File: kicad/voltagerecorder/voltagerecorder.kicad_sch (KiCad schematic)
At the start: 87 parts, among them J1 Conn_02x10_Odd_Even, J10 Conn_01x02, J11 USB_C_Receptacle_USB2.0, J12 USB_C_Receptacle_USB2.0, J14 Conn_01x08, J15 Conn_01x02, J2 Conn_01x05, J3 Conn_01x08, J8 Conn_01x05, P1 DM3CS-SF, SW1 SW_Push, U1 Opamp_Quad, U5 ADS8638, U6 STM32G473CBT6, U8 ESP32-C3-WROOM-02, U9 ESP-PSRAM32, Y1 32.768kHz, Y2 24MHz

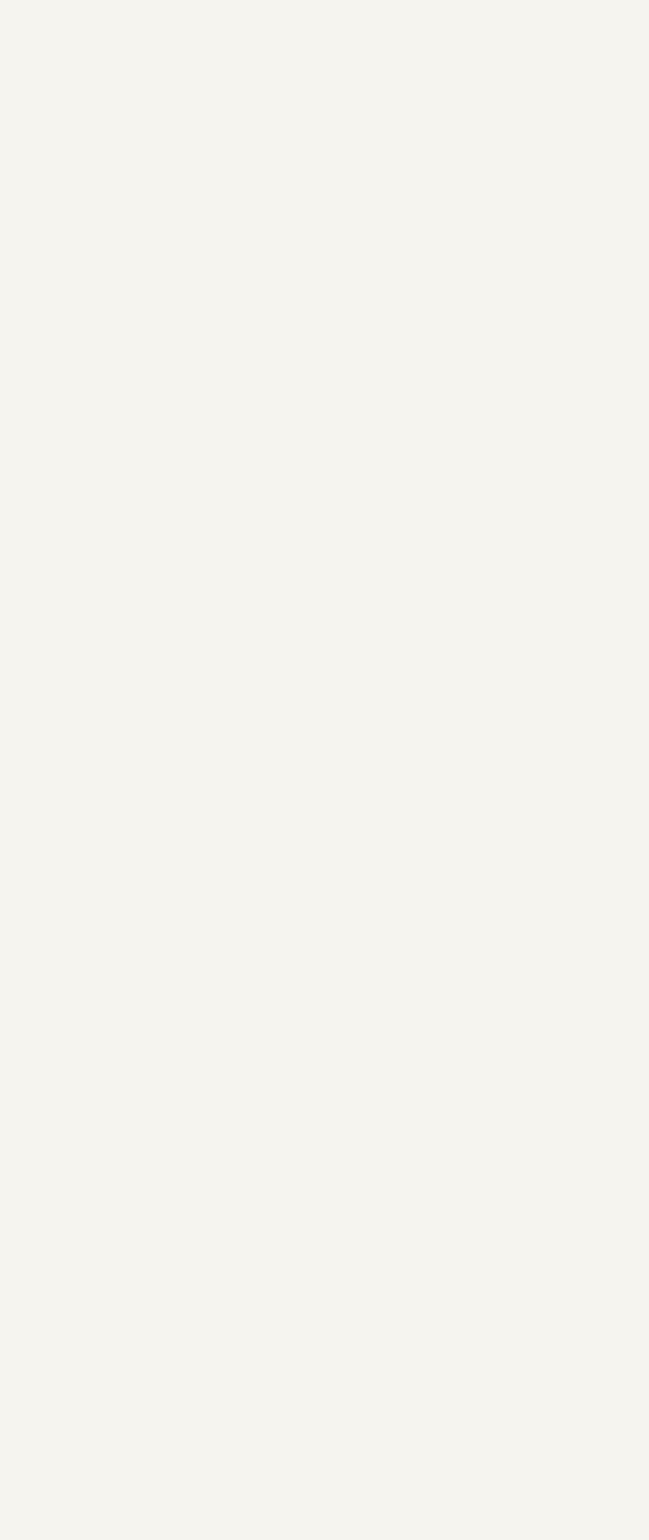
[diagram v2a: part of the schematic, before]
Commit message: vor entfernung von g4
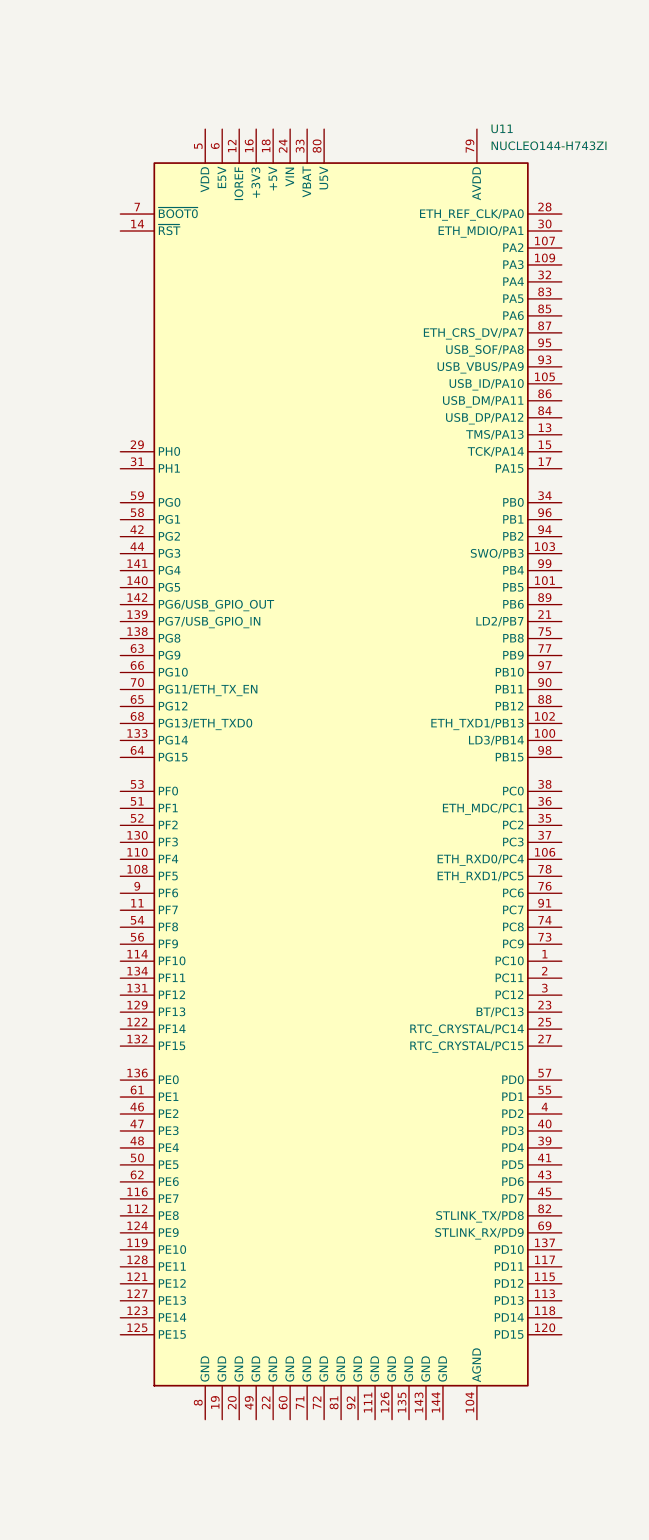
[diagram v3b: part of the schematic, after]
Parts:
- added U11: NUCLEO144-H743ZI, Module:ST_Morpho_Connector_144_STLink, symbol MCU_Module:NUCLEO144-H743ZI
- J14: footprint Connector_PinHeader_2.54mm:PinHeader_1x08_P2.54mm_Horizontal -> Connector_PinHeader_2.54mm:PinHeader_1x08_P2.54mm_Vertical
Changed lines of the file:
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@@
     (pin "1")
   )
+  (symbol (lib_id "MCU_Module:NUCLEO144-H743ZI") (at 491.49 162.56 0) (unit 1)
+    (in_bom yes) (on_board yes) (fields_autoplaced)
+    (property "Reference" "U11" (id 0) (at 513.8294 66.04 0)
+      (effects (font (size 1.27 1.27)) (justify left))
+    )
+    (property "Value" "NUCLEO144-H743ZI" (id 1) (at 513.8294 68.58 0)
+      (effects (font (size 1.27 1.27)) (justify left))
+    )
+    (property "Footprint" "Module:ST_Morpho_Connector_144_STLink" (id 2) (at 513.08 255.27 0)
+      (effects (font (size 1.27 1.27)) (justify left) hide)
+    )
+    (property "Datasheet" "https://www.st.com/resource/en/user_manual/dm00244518-stm32-nucleo144-boards-stmicroelectronics.pdf" (id 3) (at 468.63 154.94 0)
+      (effects (font (size 1.27 1.27)) hide)
+    )
+    (pin "1")
+    (pin "10")
+    (pin "100")
+    (pin "101")
+    (pin "102")
+    (pin "103")
+    (pin "104")
+    (pin "105")
+    (pin "106")
+    (pin "107")
+    (pin "108")
+    (pin "109")
+    (pin "11")
+    (pin "110")
+    (pin "111")
+    (pin "112")
+    (pin "113")
+    (pin "114")
+    (pin "115")
+    (pin "116")
+    (pin "117")
+    (pin "118")
+    (pin "119")
+    (pin "12")
+    (pin "120")
+    (pin "121")
+    (pin "122")
+    (pin "123")
+    (pin "124")
+    (pin "125")
+    (pin "126")
+    (pin "127")
+    (pin "128")
+    (pin "129")
+    (pin "13")
+    (pin "130")
+    (pin "131")
+    (pin "132")
+    (pin "133")
+    (pin "134")
+    (pin "135")
+    (pin "136")
+    (pin "137")
+    (pin "138")
+    (pin "139")
+    (pin "14")
+    (pin "140")
+    (pin "141")
+    (pin "142")
+    (pin "143")
+    (pin "144")
+    (pin "15")
+    (pin "16")
+    (pin "17")
+    (pin "18")
+    (pin "19")
+    (pin "2")
+    (pin "20")
+    (pin "21")
+    (pin "22")
+    (pin "23")
+    (pin "24")
+    (pin "25")
+    (pin "26")
+    (pin "27")
+    (pin "28")
+    (pin "29")
+    (pin "3")
+    (pin "30")
+    (pin "31")
+    (pin "32")
+    (pin "33")
+    (pin "34")
+    (pin "35")
+    (pin "36")
+    (pin "37")
+    (pin "38")
+    (pin "39")
+    (pin "4")
+    (pin "40")
+    (pin "41")
+    (pin "42")
+    (pin "43")
+    (pin "44")
+    (pin "45")
+    (pin "46")
+    (pin "47")
+    (pin "48")
+    (pin "49")
+    (pin "5")
+    (pin "50")
+    (pin "51")
+    (pin "52")
+    (pin "53")
+    (pin "54")
+    (pin "55")
+    (pin "56")
+    (pin "57")
+    (pin "58")
+    (pin "59")
+    (pin "6")
+    (pin "60")
+    (pin "61")
+    (pin "62")
+    (pin "63")
+    (pin "64")
+    (pin "65")
+    (pin "66")
+    (pin "67")
+    (pin "68")
+    (pin "69")
+    (pin "7")
+    (pin "70")
+    (pin "71")
+    (pin "72")
+    (pin "73")
+    (pin "74")
+    (pin "75")
+    (pin "76")
+    (pin "77")
+    (pin "78")
+    (pin "79")
+    (pin "8")
+    (pin "80")
+    (pin "81")
+    (pin "82")
+    (pin "83")
+    (pin "84")
+    (pin "85")
+    (pin "86")
+    (pin "87")
+    (pin "88")
+    (pin "89")
+    (pin "9")
+    (pin "90")
+    (pin "91")
+    (pin "92")
+    (pin "93")
+    (pin "94")
+    (pin "95")
+    (pin "96")
+    (pin "97")
+    (pin "98")
+    (pin "99")
+  )
   (symbol (lib_id "power:+3.3V") (at 228.6 34.29 0) (unit 1)
     (in_bom yes) (on_board yes)
@@
       (effects (font (size 1.27 1.27)) (justify left))
     )
-    (property "Footprint" "Connector_PinHeader_2.54mm:PinHeader_1x08_P2.54mm_Horizontal" (id 2) (at 382.27 219.71 0)
+    (property "Footprint" "Connector_PinHeader_2.54mm:PinHeader_1x08_P2.54mm_Vertical" (id 2) (at 382.27 219.71 0)
       (effects (font (size 1.27 1.27)) hide)
     )
@@
     )
     (path "/8331d2a5-60ce-4251-b291-6a010f9e22e4"
-      (reference "J14") (unit 1) (value "Conn_01x08") (footprint "Connector_PinHeader_2.54mm:PinHeader_1x08_P2.54mm_Horizontal")
+      (reference "J14") (unit 1) (value "Conn_01x08") (footprint "Connector_PinHeader_2.54mm:PinHeader_1x08_P2.54mm_Vertical")
     )
     (path "/21ab1728-4f5c-4275-af88-767c108866e3"
@@
       (reference "U10") (unit 1) (value "P78E-1000") (footprint "Converter_DCDC:Converter_DCDC_RECOM_R-78E-0.5_THT")
     )
+    (path "/05dd043c-c4ef-4494-8566-1770a96f93ab"
+      (reference "U11") (unit 1) (value "NUCLEO144-H743ZI") (footprint "Module:ST_Morpho_Connector_144_STLink")
+    )
     (path "/87db9c7f-6153-41e9-a246-2221486ffc84"

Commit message: G4 entfernt, I2C EEPROM hinzugefügt
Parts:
- removed BT1: Battery_Cell, Battery:BatteryHolder_Keystone_500, symbol Device:Battery_Cell
- removed C29, C30, C32, C37, C38, C39: 100n, Capacitor_SMD:C_0603_1608Metric_Pad1.08x0.95mm_HandSolder, symbol Device:C
- removed C31, C40: 1u, Capacitor_SMD:C_0603_1608Metric_Pad1.08x0.95mm_HandSolder, symbol Device:C
- removed C36: 10u, Capacitor_SMD:C_0805_2012Metric_Pad1.18x1.45mm_HandSolder, symbol Device:C
- removed C41, C42, C43, C44: 22pF, Capacitor_SMD:C_0603_1608Metric_Pad1.08x0.95mm_HandSolder, symbol Device:C
- removed C46, C47: 10nF, Capacitor_SMD:C_0603_1608Metric_Pad1.08x0.95mm_HandSolder, symbol Device:C
- removed D10, D11, D12, D5, D6, D7, D8: D_Zener, Diode_SMD:D_SOD-323_HandSoldering, symbol Device:D_Zener
- removed D13: RED, Diode_SMD:D_0603_1608Metric, symbol Device:LED_Filled
- removed D14: GREEN, Diode_SMD:D_0603_1608Metric, symbol Device:LED_Filled
- removed H5, H6: MountingHole_Pad, MountingHole:MountingHole_3.2mm_M3_DIN965_Pad, symbol Mechanical:MountingHole_Pad
- removed J10: Conn_01x02, Connector_PinHeader_2.54mm:PinHeader_1x02_P2.54mm_Vertical, symbol Connector_Generic:Conn_01x02
- removed J11, J12: USB_C_Receptacle_USB2.0, Connector_USB:USB_C_Receptacle_XKB_U262-16XN-4BVC11, symbol Connector:USB_C_Receptacle_USB2.0
- removed J14, J3: Conn_01x08, Connector_PinHeader_2.54mm:PinHeader_1x08_P2.54mm_Vertical, symbol Connector_Generic:Conn_01x08
- removed J8: Conn_01x05, Connector_PinHeader_2.54mm:PinHeader_1x05_P2.54mm_Vertical, symbol Connector_Generic:Conn_01x05
- removed P1: DM3CS-SF, Hirose:HRS_DM3CS-SF, symbol Hirose:DM3CS-SF
- removed R34, R35, R36, R38, R39, R44, R47: 10k, Resistor_SMD:R_0603_1608Metric_Pad0.98x0.95mm_HandSolder, symbol Device:R
- removed R46, R48: 1M, Resistor_SMD:R_0603_1608Metric, symbol Device:R
- removed R49, R50: 1k, Resistor_SMD:R_0603_1608Metric, symbol Device:R
- removed SW1: SW_Push, Button_Switch_SMD:SW_Tactile_SPST_NO_Straight_CK_PTS636Sx25SMTRLFS, symbol Switch:SW_Push
- removed U11: NUCLEO144-H743ZI, Module:ST_Morpho_Connector_144_STLink, symbol MCU_Module:NUCLEO144-H743ZI
- removed U6: STM32G473CBT6, Package_QFP:LQFP-48_7x7mm_P0.5mm, symbol wittmann:STM32G473CBT6
- removed U8: ESP32-C3-WROOM-02, Espressif:ESP32-C3-WROOM-02, symbol espressif:ESP32-C3-WROOM-02
- removed U9: ESP-PSRAM32, Package_SO:SOIC-8_3.9x4.9mm_P1.27mm, symbol Memory_RAM:ESP-PSRAM32
- removed Y1: 32.768kHz, Crystal:Crystal_SMD_3225-4Pin_3.2x2.5mm, symbol Device:Crystal_GND24
- removed Y2: 24MHz, Crystal:Crystal_SMD_3225-4Pin_3.2x2.5mm, symbol Device:Crystal_GND24
- added J3: Conn_02x07_Odd_Even, Connector_PinHeader_2.54mm:PinHeader_2x07_P2.54mm_Horizontal, symbol Connector_Generic:Conn_02x07_Odd_Even
- added JP6: SolderJumper_2_Open, Jumper:SolderJumper-2_P1.3mm_Open_RoundedPad1.0x1.5mm, symbol Jumper:SolderJumper_2_Open
- added U6: AT24CS08-STUM, Package_TO_SOT_SMD:SOT-23-5, symbol Memory_EEPROM:AT24CS08-STUM
- C24: value 100n -> 1u
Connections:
- net BOOT0 is gone; now on net +3.3V: R3.2
- net G4_NRST is gone; now on net GND: R32.1
- net G4_PA4 is gone; now on net IN3_EXT: J1.19 (Pin_19)
- net G4_PA5 is gone; now on net IN7_EXT: J1.20 (Pin_20)
- net SHIELD is gone; now on net GND: H1.1, H2.1, H3.1, H4.1
- net +3.3V: now also J3.10 (Pin_10), J3.9 (Pin_9), JP6.2 (B), U6.4 (VCC); no longer R32.2
- net +5V: now also J3.11 (Pin_11), J3.12 (Pin_12)
- net AL_PD: now also J3.6 (Pin_6)
- net CS: now also J3.7 (Pin_7)
- net GND: now also J3.13 (Pin_13), J3.14 (Pin_14), U6.2 (GND); no longer R3.1
- net IN0_EXT: now also J1.13 (Pin_13); no longer J1.11 (Pin_11)
- net IN1_EXT: now also J1.15 (Pin_15); no longer J1.13 (Pin_13)
- net IN2_EXT: now also J1.17 (Pin_17); no longer J1.15 (Pin_15)
- net IN3_EXT: no longer J1.17 (Pin_17)
- net IN4_EXT: now also J1.14 (Pin_14); no longer J1.12 (Pin_12)
- net IN5_EXT: now also J1.16 (Pin_16); no longer J1.14 (Pin_14)
- net IN6_EXT: now also J1.18 (Pin_18); no longer J1.16 (Pin_16)
- net IN7_EXT: no longer J1.18 (Pin_18)
- net MISO: now also J3.5 (Pin_5)
- net MOSI: now also J3.3 (Pin_3)
- net REF_EXT: now also J1.11 (Pin_11); no longer J1.10 (Pin_10)
- net SCLK: now also J3.1 (Pin_1)
- net SENSE_5V: now also J3.8 (Pin_8)
- net SPI3_MOSI renamed I2C_SCL
- net I2C_SCL: now also J1.12 (Pin_12), J3.2 (Pin_2), U6.1 (SCL)
- new net: JP6.1 (A), R32.2, U6.5 (WP)
- new net I2C_SDA: J1.10 (Pin_10), J3.4 (Pin_4), R3.1, U6.3 (SDA)
- no-connect marks 3 -> 0
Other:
- note added: "closed->write protected"
- note added: "für EEPROM"
- note removed: "ADC2_IN12"
- note removed: "CR1225"
- note removed: "DAC1_OUT1"
- note removed: "DAC1_OUT2"
- note removed: "DAC2_OUT1"
- note removed: "QuadSPI verwenden?"
- note removed: "TIM1_CH1N"
- note removed: "TVS Dioden 3.3V unidir"
- note removed: "TVS Dioden 3.3V unidir 15pF ist ok"
- note removed: "TVS Dioden 5V unidir"
- note removed: "USART1_RX"
- note removed: "USART1_TX"
- note removed: "für G4"
- moved on the sheet: C1, C10, C11, C12, C13, C14, C2, C22, C26, C28, C3, C4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
